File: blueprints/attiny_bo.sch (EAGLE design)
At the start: 8 parts, among them IC1 ATTiny85, J1 AVR_SPI_PRG_6NS

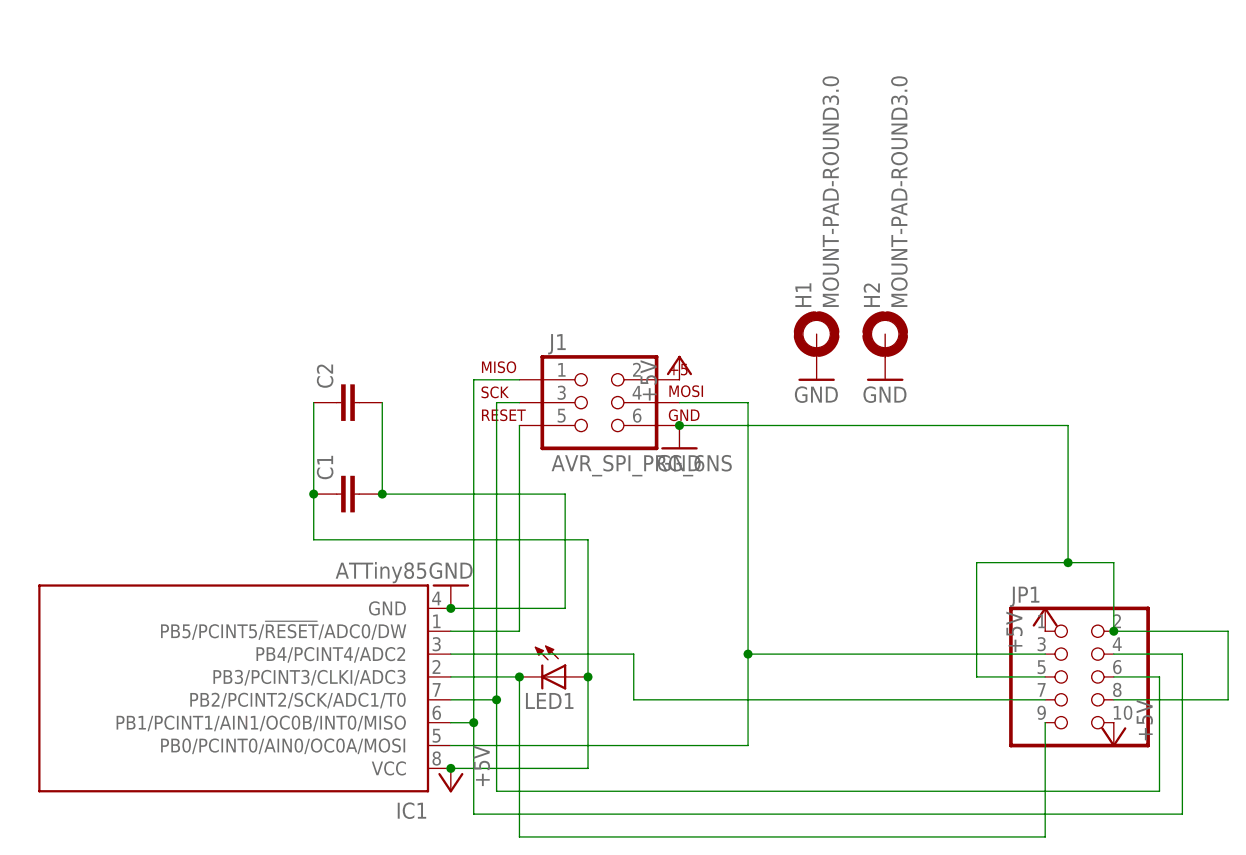
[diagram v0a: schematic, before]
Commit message: started adding optional crystal to the board
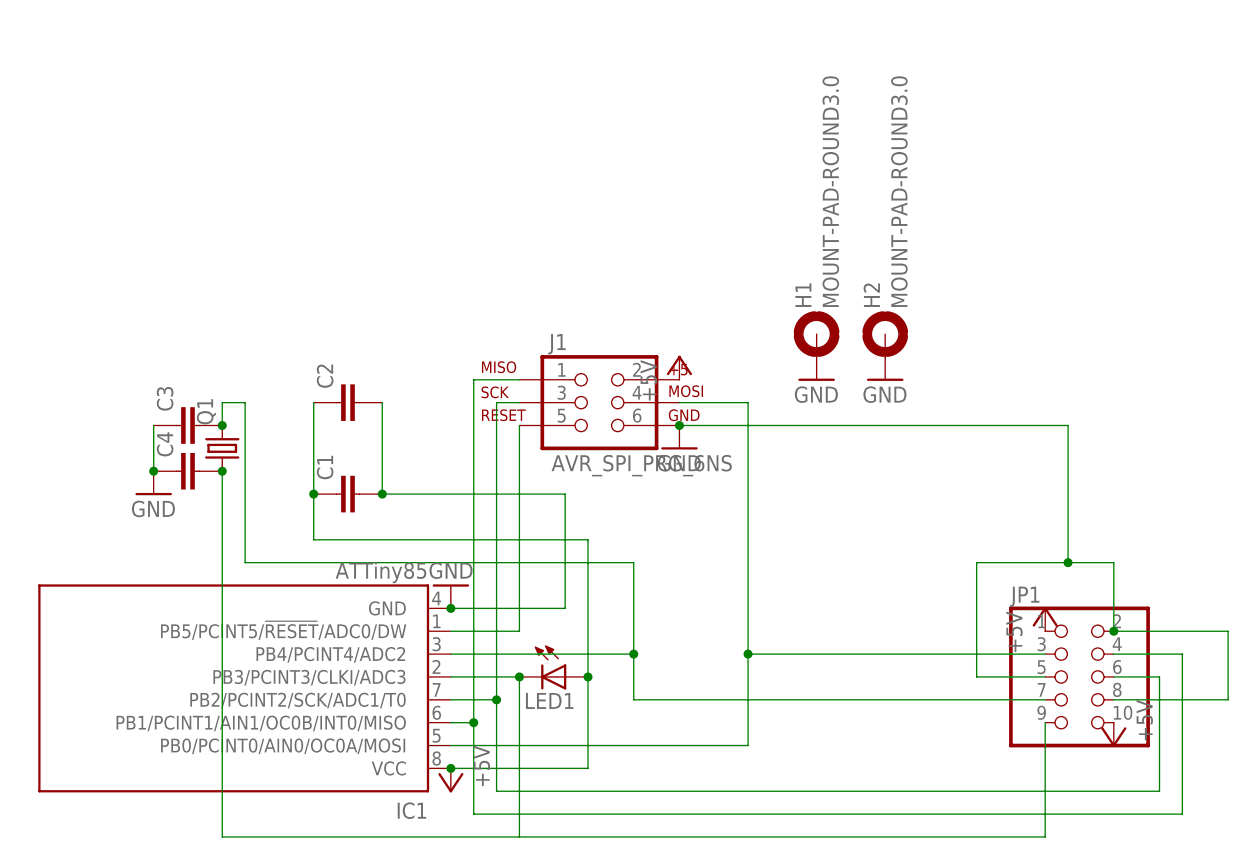
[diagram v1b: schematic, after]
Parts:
- added C3, C4: (no value), rcl:C-EUC0603
- added Q1: (no value), crystal:CRYSTALSM49
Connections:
- net GND: now also C3.1, C4.1
- net PB3: now also C4.2, Q1.1
- net PB4: now also C3.2, Q1.2
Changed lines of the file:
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@@
 <part name="P+1" library="supply1" deviceset="+5V" device=""/>
 <part name="P+2" library="supply1" deviceset="+5V" device=""/>
+<part name="Q1" library="crystal" deviceset="CRYSTAL" device="SM49"/>
+<part name="C3" library="rcl" deviceset="C-EU" device="C0603"/>
+<part name="C4" library="rcl" deviceset="C-EU" device="C0603"/>
+<part name="GND4" library="supply1" deviceset="GND" device=""/>
 </parts>
 <sheets>
@@
 <instance part="P+1" gate="1" x="116.84" y="83.82"/>
 <instance part="P+2" gate="1" x="124.46" y="68.58" rot="R180"/>
+<instance part="Q1" gate="G$1" x="25.4" y="101.6" rot="R90"/>
+<instance part="C3" gate="G$1" x="20.32" y="104.14" rot="R90"/>
+<instance part="C4" gate="G$1" x="20.32" y="99.06" rot="R90"/>
+<instance part="GND4" gate="1" x="17.78" y="96.52"/>
 </instances>
 <busses>
@@
 <pinref part="GND2" gate="1" pin="GND"/>
 </segment>
+<segment>
+<pinref part="C4" gate="G$1" pin="1"/>
+<pinref part="GND4" gate="1" pin="GND"/>
+<pinref part="C3" gate="G$1" pin="1"/>
+<wire x1="17.78" y1="104.14" x2="17.78" y2="99.06" width="0.1524" layer="91"/>
+<junction x="17.78" y="99.06"/>
+</segment>
 </net>
 <net name="+5V" class="1">
@@
 <wire x1="116.84" y1="58.42" x2="116.84" y2="71.12" width="0.1524" layer="91"/>
 <junction x="58.42" y="76.2"/>
+<pinref part="Q1" gate="G$1" pin="1"/>
+<pinref part="C4" gate="G$1" pin="2"/>
+<wire x1="58.42" y1="58.42" x2="25.4" y2="58.42" width="0.1524" layer="91"/>
+<wire x1="25.4" y1="58.42" x2="25.4" y2="99.06" width="0.1524" layer="91"/>
+<junction x="25.4" y="99.06"/>
 </segment>
 </net>
@@
 <pinref part="JP1" gate="A" pin="7"/>
 <wire x1="71.12" y1="73.66" x2="116.84" y2="73.66" width="0.1524" layer="91"/>
-</segment>
-</net>
+<wire x1="71.12" y1="78.74" x2="71.12" y2="88.9" width="0.1524" layer="91"/>
+<wire x1="71.12" y1="88.9" x2="27.94" y2="88.9" width="0.1524" layer="91"/>
+<wire x1="27.94" y1="88.9" x2="27.94" y2="106.68" width="0.1524" layer="91"/>
+<pinref part="Q1" gate="G$1" pin="2"/>
+<pinref part="C3" gate="G$1" pin="2"/>
+<wire x1="27.94" y1="106.68" x2="25.4" y2="106.68" width="0.1524" layer="91"/>
+<wire x1="25.4" y1="106.68" x2="25.4" y2="104.14" width="0.1524" layer="91"/>
+<junction x="71.12" y="78.74"/>
+<junction x="25.4" y="104.14"/>
+</segment>
+</net>

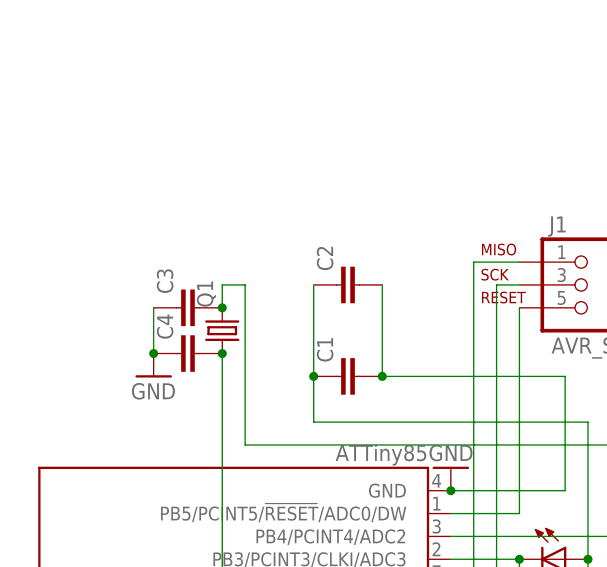
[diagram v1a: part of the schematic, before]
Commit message: started adding optional crystal to the board
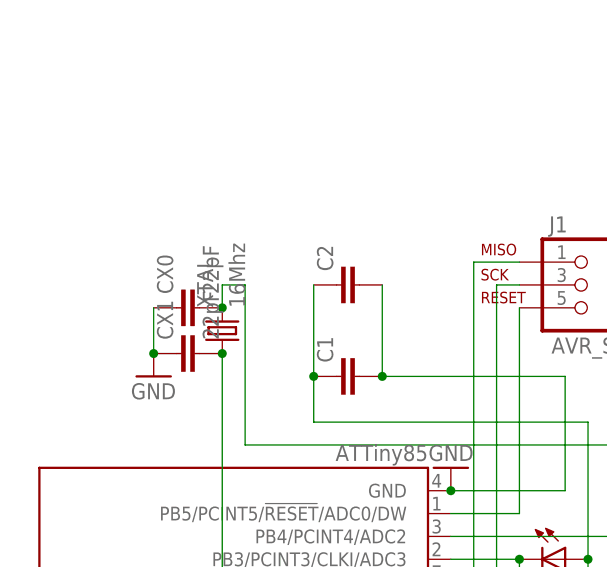
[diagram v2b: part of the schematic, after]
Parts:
- removed Q1: (no value), crystal:CRYSTALSM49
- added XTAL: 16Mhz, crystal:CRYSTALCTS406
- CX0, CX1: value (none) -> 22pF
- renumbered C3 to CX0, C4 to CX1
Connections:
- net PB3: now also XTAL.1; no longer Q1.1
- net PB4: now also XTAL.2; no longer Q1.2
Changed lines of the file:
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@@
 <part name="P+1" library="supply1" deviceset="+5V" device=""/>
 <part name="P+2" library="supply1" deviceset="+5V" device=""/>
-<part name="Q1" library="crystal" deviceset="CRYSTAL" device="SM49"/>
-<part name="C3" library="rcl" deviceset="C-EU" device="C0603"/>
-<part name="C4" library="rcl" deviceset="C-EU" device="C0603"/>
+<part name="CX0" library="rcl" deviceset="C-EU" device="C0603" value="22pF"/>
+<part name="CX1" library="rcl" deviceset="C-EU" device="C0603" value="22pF"/>
 <part name="GND4" library="supply1" deviceset="GND" device=""/>
+<part name="XTAL" library="crystal" deviceset="CRYSTAL" device="CTS406" value="16Mhz"/>
 </parts>
 <sheets>
@@
 <instance part="P+1" gate="1" x="116.84" y="83.82"/>
 <instance part="P+2" gate="1" x="124.46" y="68.58" rot="R180"/>
-<instance part="Q1" gate="G$1" x="25.4" y="101.6" rot="R90"/>
-<instance part="C3" gate="G$1" x="20.32" y="104.14" rot="R90"/>
-<instance part="C4" gate="G$1" x="20.32" y="99.06" rot="R90"/>
+<instance part="CX0" gate="G$1" x="20.32" y="104.14" rot="R90"/>
+<instance part="CX1" gate="G$1" x="20.32" y="99.06" rot="R90"/>
 <instance part="GND4" gate="1" x="17.78" y="96.52"/>
+<instance part="XTAL" gate="G$1" x="25.4" y="101.6" rot="R90"/>
 </instances>
 <busses>
@@
 </segment>
 <segment>
-<pinref part="C4" gate="G$1" pin="1"/>
+<pinref part="CX1" gate="G$1" pin="1"/>
 <pinref part="GND4" gate="1" pin="GND"/>
-<pinref part="C3" gate="G$1" pin="1"/>
+<pinref part="CX0" gate="G$1" pin="1"/>
 <wire x1="17.78" y1="104.14" x2="17.78" y2="99.06" width="0.1524" layer="91"/>
 <junction x="17.78" y="99.06"/>
@@
 <wire x1="116.84" y1="58.42" x2="116.84" y2="71.12" width="0.1524" layer="91"/>
 <junction x="58.42" y="76.2"/>
-<pinref part="Q1" gate="G$1" pin="1"/>
-<pinref part="C4" gate="G$1" pin="2"/>
+<pinref part="CX1" gate="G$1" pin="2"/>
 <wire x1="58.42" y1="58.42" x2="25.4" y2="58.42" width="0.1524" layer="91"/>
 <wire x1="25.4" y1="58.42" x2="25.4" y2="99.06" width="0.1524" layer="91"/>
+<pinref part="XTAL" gate="G$1" pin="1"/>
 <junction x="25.4" y="99.06"/>
 </segment>
@@
 <wire x1="71.12" y1="88.9" x2="27.94" y2="88.9" width="0.1524" layer="91"/>
 <wire x1="27.94" y1="88.9" x2="27.94" y2="106.68" width="0.1524" layer="91"/>
-<pinref part="Q1" gate="G$1" pin="2"/>
-<pinref part="C3" gate="G$1" pin="2"/>
+<pinref part="CX0" gate="G$1" pin="2"/>
 <wire x1="27.94" y1="106.68" x2="25.4" y2="106.68" width="0.1524" layer="91"/>
 <wire x1="25.4" y1="106.68" x2="25.4" y2="104.14" width="0.1524" layer="91"/>
 <junction x="71.12" y="78.74"/>
+<pinref part="XTAL" gate="G$1" pin="2"/>
 <junction x="25.4" y="104.14"/>
 </segment>
